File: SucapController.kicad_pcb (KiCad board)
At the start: 2 copper layers, 39.2 x 30.4 mm, 44 parts, among them J1 Conn_01x14, J2 Conn_01x04, J3 Conn_01x02, J4 Conn_02x03_Counter_Clockwise, J5 Conn_02x03_Counter_Clockwise, J6 Conn_02x03_Counter_Clockwise, J7 Screw_Terminal_01x01, Q1 SL2301, U1 HX9193, U2 HX9193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

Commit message: Do some change
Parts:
- removed Ce: 2.2u, Capacitor_SMD:C_0603_1608Metric
- removed D1: LED, LED_SMD:LED_0603_1608Metric
- removed J2: Conn_01x04, Connector_JST:JST_GH_SM04B-GHS-TB_1x04-1MP_P1.25mm_Horizontal
- added C19: 100n, GENERAL_RCL_SMD:C0603(1608M), F.Cu at (225.2, 97.7)
- C1, C11, C12, C13, C18, C2, C3, C4, C5, C6, C8, C9: footprint Capacitor_SMD:C_0603_1608Metric -> GENERAL_RCL_SMD:C0603(1608M)
- C17: value 100n -> 2.2u; footprint Capacitor_SMD:C_0603_1608Metric -> GENERAL_RCL_SMD:C0603(1608M)
- C7: footprint Capacitor_SMD:C_0603_1608Metric -> GENERAL_RCL_SMD:C0603(1608M); moved to F.Cu
- Q1: value SL2301 -> SI2301
- R1: value 10K -> 100n; footprint Resistor_SMD:R_0603_1608Metric -> GENERAL_RCL_SMD:R0603(1608M)
- R3: value 1K -> 1k; footprint Resistor_SMD:R_0603_1608Metric -> GENERAL_RCL_SMD:R0603(1608M)
- U1: value HX9193 -> HX9193-33GB; footprint Package_TO_SOT_SMD:SOT-23-5_HandSoldering -> GENERAL_SMALL-SEMI_SMD:SOT-23-5
- U4: value STM32H750VBTx -> STM32H750VBT6; footprint Package_QFP:LQFP-100_14x14mm_P0.5mm -> GENERAL_LARGE-SEMI_SMD:QFP-1414_100
- moved C13 59.8 mm to (249.0, 92.9), turned to 0 degrees
- moved C9 50.9 mm to (241.3, 95.4), turned to 0 degrees
- moved C11 46.5 mm to (237.8, 97.2), turned to 0 degrees
- moved C6 45.5 mm to (244.8, 98.0), turned to 0 degrees
- moved C3 45.3 mm to (241.3, 100.5), turned to 0 degrees
- moved C1 42.8 mm to (241.3, 98.0), turned to 0 degrees
- moved C2 41.7 mm to (229.8, 105.3)
- moved C18 38.7 mm to (244.8, 95.4), turned to 0 degrees
- moved C4 38.5 mm to (248.3, 95.4), turned to 0 degrees
- moved C5 24.7 mm to (237.8, 99.7), turned to 0 degrees
- moved C17 23.2 mm to (208.9, 110.3), turned to 180 degrees
- moved C7 20.7 mm to (214.2, 92.4), turned to 180 degrees
- moved C12 10.5 mm to (178.3, 107.4), turned to 0 degrees
- moved R1 6.88 mm to (198.7, 96.3), turned to 90 degrees
- moved U1 0.53 mm to (188.8, 108.8), turned to -90 degrees
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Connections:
- C17 pad 1: GND -> Net-(U4-Pad48)
- C17 pad 2: /RESET -> GND
- C18 pad 1: Net-(C18-Pad1) -> Net-(U4-Pad73)
- R1 pad 1: /RESET -> Net-(U4-Pad14)
- R3 pad 1: +3V3 -> Net-(D1-Pad2)
- R3 pad 2: Net-(D1-Pad2) -> +3V3
- U4 pad 14: /RESET -> Net-(U4-Pad14)
- U4 pad 48: Net-(C18-Pad1) -> Net-(U4-Pad48)
- U4 pad 73: Net-(C19-Pad1) -> Net-(U4-Pad73)
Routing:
- net Net-(U4-Pad48): track 0.00 -> 2.70 mm
- net Net-(C18-Pad1): track 2.70 -> 0.00 mm
- net Net-(U4-Pad73): track 0.00 -> 2.26 mm
- net Net-(C19-Pad1): track 2.26 -> 0.00 mm
- net +5V: track 63.8 -> 64.4 mm

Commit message: do some change
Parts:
- added D1: LED, GENERAL_2-PIN_PLASTIC_SMD:LED0603(1608M), F.Cu at (188.1, 98.2)
- C10, C14, C15, C16, C20, C21, C22: footprint Capacitor_SMD:C_0603_1608Metric -> GENERAL_RCL_SMD:C0603(1608M)
- C6: moved to B.Cu
- R2: footprint Resistor_SMD:R_0603_1608Metric -> GENERAL_RCL_SMD:R0603(1608M)
- U2: footprint Package_TO_SOT_SMD:SOT-23-5_HandSoldering -> GENERAL_SMALL-SEMI_SMD:SOT-23-5
- U3: footprint Package_SO:SOIC-8_5.23x5.23mm_P1.27mm -> GENERAL_MIDDLE-SEMI_SMD:SOIC-5252_8
- moved C13 61.6 mm to (188.5, 105.0), turned to -90 degrees
- moved C9 50.8 mm to (192.9, 110.8), turned to 180 degrees
- moved C4 48.5 mm to (200.1, 89.9), turned to 180 degrees
- moved C6 47.0 mm to (198.4, 105.8)
- moved C11 46.5 mm to (192.8, 109.2), turned to 180 degrees
- moved C1 45.9 mm to (196.5, 108.1), turned to 90 degrees
- moved C2 41.7 mm to (190.9, 90.6)
- moved C5 39.0 mm to (200.3, 110.4), turned to 180 degrees
- moved C3 30.1 mm to (212.4, 109.1), turned to 90 degrees
- moved C18 29.4 mm to (215.4, 94.4)
- moved C19 28.7 mm to (197.5, 90.2), turned to -90 degrees
- moved C12 12.2 mm to (190.3, 105.0), turned to -90 degrees
- moved R1 6.88 mm to (195.1, 90.4), turned to 180 degrees
- moved C20 1.68 mm to (201.2, 95.6), turned to 0 degrees
- turned U2 to -90 degrees
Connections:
- net Net-(U4-Pad14) renamed /RNSET
- C23 pad 1: GND -> /OSC32_IN
- C23 pad 2: /OSC32_IN -> GND
- C24 pad 1: GND -> /OSC32_OUT
- C24 pad 2: /OSC32_OUT -> GND
- U6 pad 4: /UART1_RX -> unconnected-(U6-Pad4)
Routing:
- net /RNSET: track 0.00 -> 24.4 mm
- net /RESET: track 24.4 -> 0.00 mm
- net GND: track 29.4 -> 17.6 mm, vias 32 -> 24
- net /OSC32_OUT: track 9.65 -> 21.4 mm, vias 0 -> 8

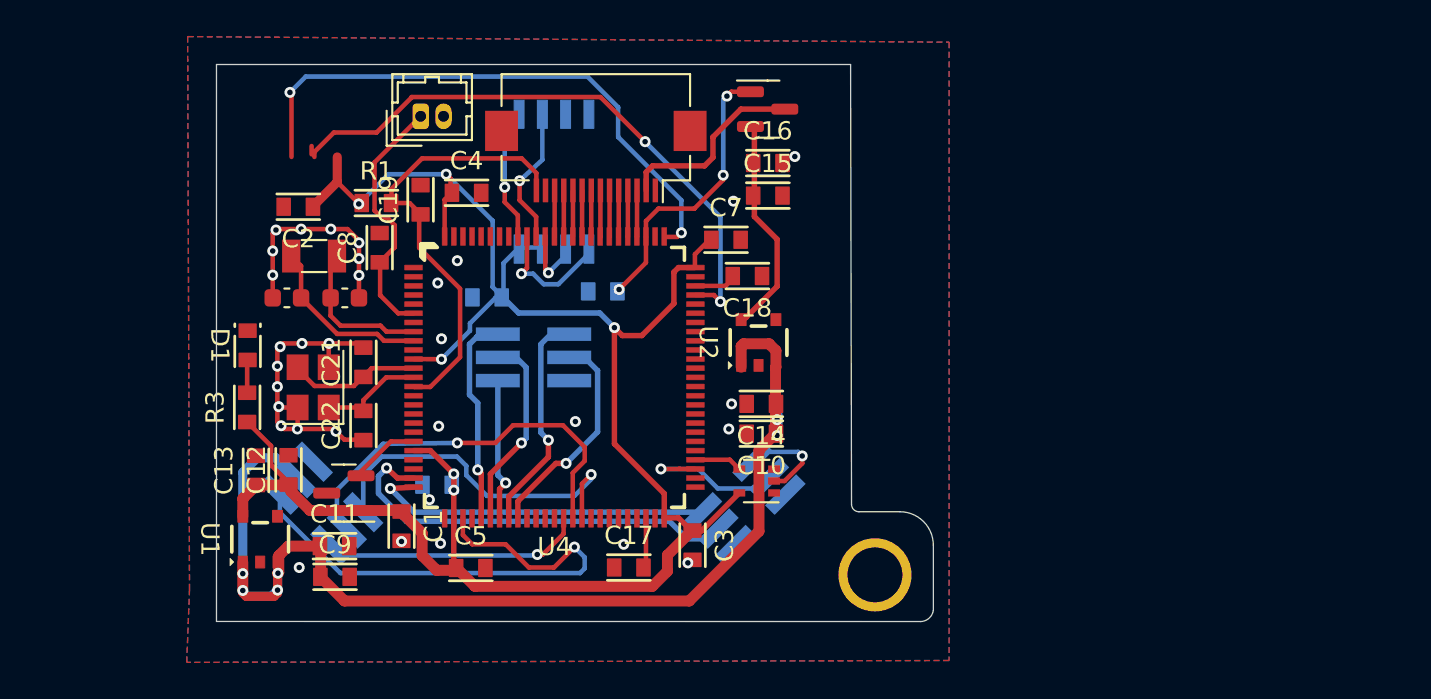
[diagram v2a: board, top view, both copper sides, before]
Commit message: Turn the footprints into ours
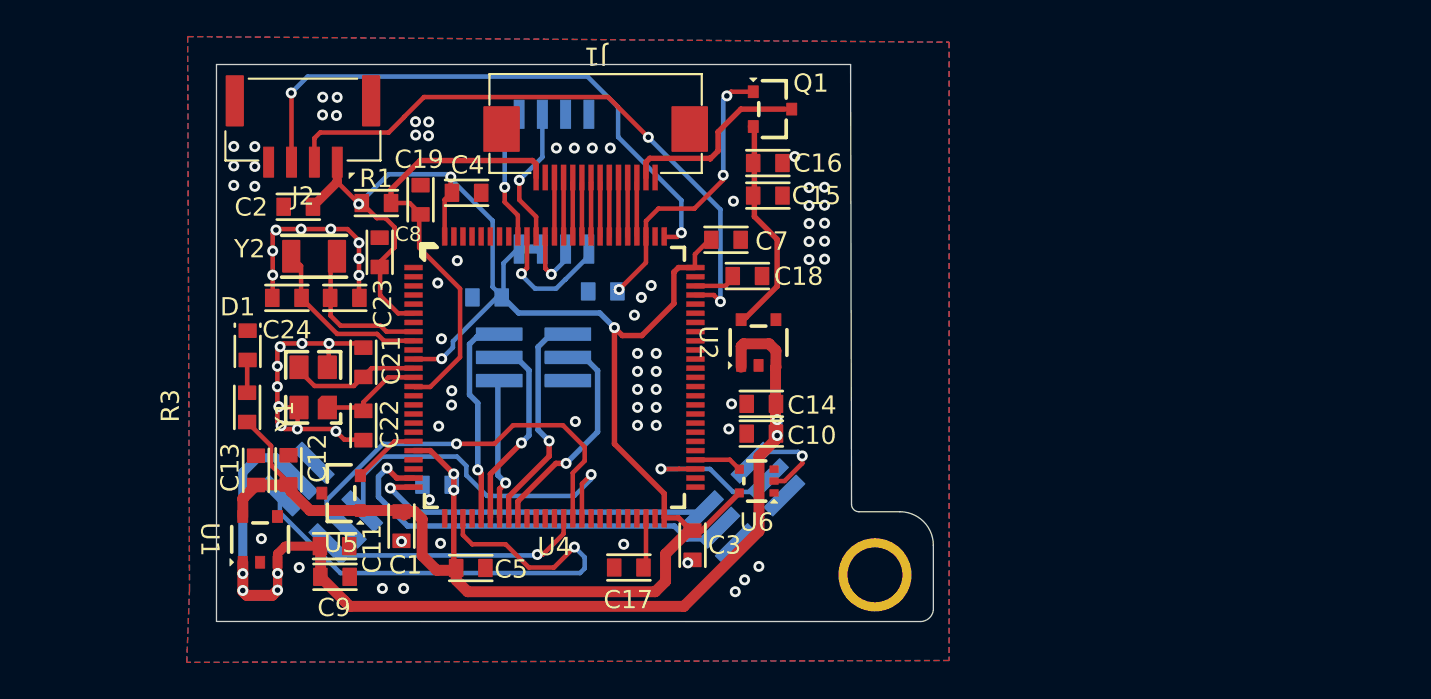
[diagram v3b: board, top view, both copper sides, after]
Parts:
- removed J3: Conn_01x02, Connector_Hirose:Hirose_DF13-02P-1.25DSA_1x02_P1.25mm_Vertical
- added J2: , CONNECTOR_GH_SMD:GH1.25_H_4, F.Cu at (191.1, 86.2)
- C23, C24: footprint Capacitor_SMD:C_0603_1608Metric -> GENERAL_RCL_SMD:C0603(1608M)
- J1: footprint Connector_FFC-FPC:Hirose_FH12-14S-0.5SH_1x14-1MP_P0.50mm_Horizontal -> MECHANICAL_EDGE-CONN:FFC_14
- J4, J5, J6: footprint Connector_PinHeader_1.27mm:PinHeader_2x03_P1.27mm_Vertical_SMD -> CONNECTOR_PINHEADER_SMD:PINHEADER_02x03_1.27mm
- Q1, U5: footprint Package_TO_SOT_SMD:SOT-23 -> GENERAL_SMALL-SEMI_SMD:SOT-23
- U6: footprint Package_TO_SOT_SMD:SOT-353_SC-70-5 -> GENERAL_SMALL-SEMI_SMD:SOT-353
- Y1: footprint Crystal:Crystal_SMD_3225-4Pin_3.2x2.5mm -> GENERAL_XTAL_OSC_SMD:SMD-3225_4
- Y2: footprint Crystal:Crystal_SMD_3215-2Pin_3.2x1.5mm -> GENERAL_XTAL_OSC_SMD:SMD-3215_2
- moved J1 1.80 mm to (207.1, 86.1)
- moved Q1 0.27 mm to (216.8, 85.3), turned to 180 degrees
- moved C8 0.25 mm to (195.3, 93.1)
- moved U5 0.15 mm to (193.2, 106.3), turned to 0 degrees
- turned U6 to 0 degrees
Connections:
- C19 pad 2: /RNSET -> /RESET
- C23 pad 1: /OSC32_IN -> GND
- C23 pad 2: GND -> /OSC32_IN
- C24 pad 1: /OSC32_OUT -> GND
- C24 pad 2: GND -> /OSC32_OUT
- C8 pad 2: +3V0 -> +3V3
- R1 pad 1: /RNSET -> /RESET
- U4 pad 14: /RNSET -> /RESET
- U4 pad 6: +3V0 -> +3V3
- U6 pad 1: (no net) -> unconnected-(U6-Pad1)
- U6 pad 4: unconnected-(U6-Pad4) -> /UART1_RX
- Y2 pad 1: /OSC32_IN -> /OSC32_OUT
- Y2 pad 2: /OSC32_OUT -> /OSC32_IN
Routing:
- net /RNSET: track 24.4 -> 0.00 mm
- net /RESET: track 0.00 -> 23.9 mm
- net +3V0: track 14.0 -> 0.00 mm
- net GND: track 17.6 -> 29.4 mm, vias 24 -> 81
- net /OSC32_OUT: track 21.4 -> 9.65 mm, vias 8 -> 0
- net +3V3: track 108.9 -> 118.9 mm
- net +5V: track 64.6 -> 63.9 mm
- net /SPI1_MOSI: track 7.08 -> 7.67 mm

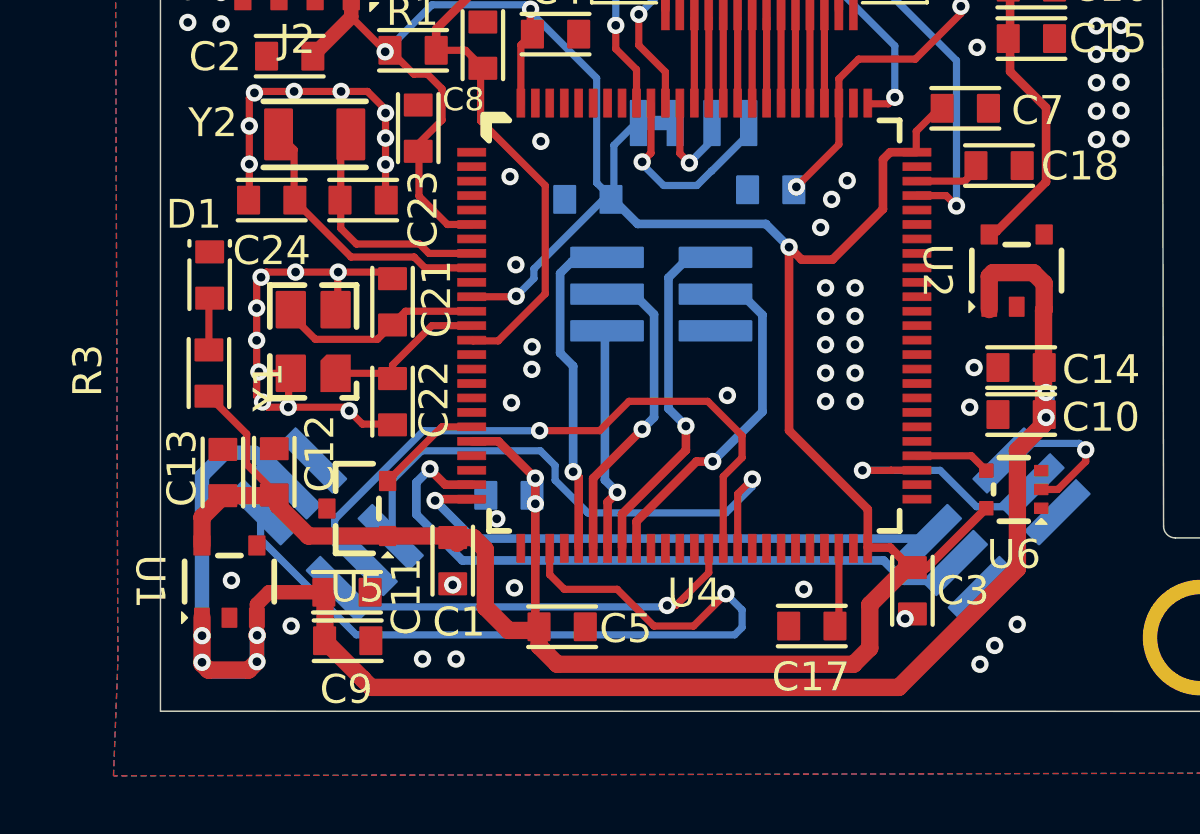
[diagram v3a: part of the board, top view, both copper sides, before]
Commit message: Turn REF3030 into TL431
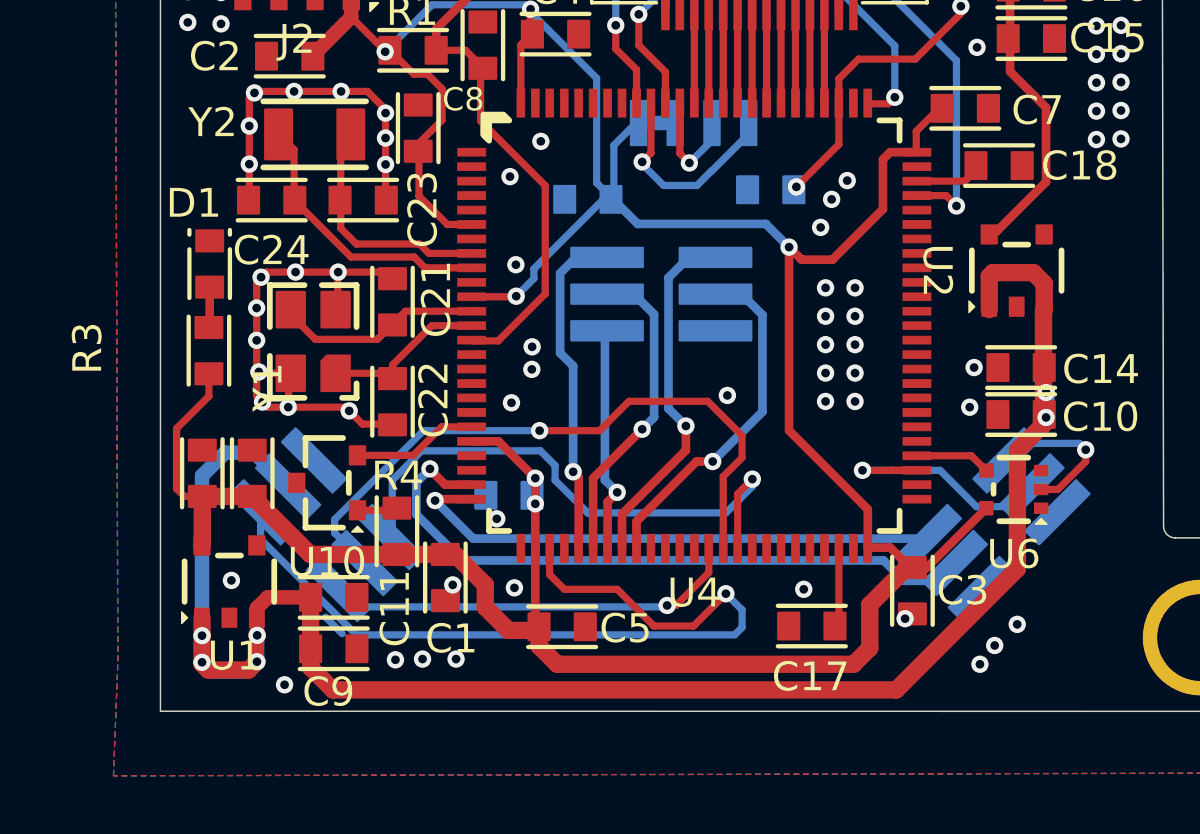
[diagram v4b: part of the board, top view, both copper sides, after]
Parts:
- removed U5: REF3030, GENERAL_SMALL-SEMI_SMD:SOT-23
- added R4: Resistor, GENERAL_RCL_SMD:R0603(1608M), F.Cu at (194.6, 107.1)
- added U10: TL431, GENERAL_SMALL-SEMI_SMD:SOT-23, F.Cu at (192.2, 105.4)
-  : renamed from C12
-  : renamed from C13
- moved R3 0.77 mm to (188.1, 100.8)
- moved   0.76 mm to (189.6, 105.1)
- moved   0.71 mm to (187.8, 105.1)
- moved C1 0.64 mm to (196.2, 108.7)
- moved C9 0.56 mm to (192.4, 111.1)
- moved C11 0.49 mm to (192.4, 109.3)
- moved D1 0.38 mm to (188.1, 97.8)
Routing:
- net Net-(U10-Pad1): track 0.00 -> 1.39 mm
- net GND: vias 81 -> 82

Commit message: fix some error
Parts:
-  : renamed from J1
-  : renamed from J7; footprint MyLib:TestPoint -> GENERAL_HOLE:HOLE-04-03_1
- C12, C13: renamed from  
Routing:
- net /EN_MOS: track 14.3 -> 13.5 mm
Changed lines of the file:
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@@
   (net 96 "Net-(J1-Pad2)")
   (net 97 "unconnected-(U6-Pad1)")
-  (net 98 "Net-(U10-Pad1)")
+  (net 98 "Net-(R4-Pad2)")
   (footprint "GENERAL_RCL_SMD:C0603(1608M)" (layer "F.Cu")
     (at 189.5602 105.0544 -90)
@@
     (property "Sheetname" "")
     (attr smd)
-    (fp_text reference " " (at -0.4318 -1.3462 90) (layer "F.SilkS")
+    (fp_text reference "C12" (at -0.4318 -1.3462 90) (layer "F.SilkS")
       (effects (font (size 1 1) (thickness 0.15)))
     )
@@
     (property "Sheetname" "")
     (attr smd)
-    (fp_text reference "J1" (at 0 3.683 180 unlocked) (layer "F.SilkS")
+    (fp_text reference " " (at 0 3.683 180 unlocked) (layer "F.SilkS")
       (effects (font (size 1 1) (thickness 0.15)))
     )
@@
     (fp_rect (start -0.65 -1.45) (end 0.65 1.45) (layer "F.Fab") (width 0.1) (fill none))
     (pad "1" smd roundrect (at 1.05 0.95 90) (size 0.7 0.6) (layers "F.Cu" "F.Paste" "F.Mask") (roundrect_rratio 0.05)
-      (net 98 "Net-(U10-Pad1)") (pinfunction "R") (pintype "power_in") (solder_mask_margin 0.05) (solder_paste_margin_ratio -0.075))
+      (net 98 "Net-(R4-Pad2)") (pinfunction "R") (pintype "power_in") (solder_mask_margin 0.05) (solder_paste_margin_ratio -0.075))
     (pad "2" smd roundrect (at 1.05 -0.95 90) (size 0.7 0.6) (layers "F.Cu" "F.Paste" "F.Mask") (roundrect_rratio 0.05)
       (net 53 "/VREF") (pinfunction "K") (pintype "power_out") (solder_mask_margin 0.05) (solder_paste_margin_ratio -0.075))
@@
     (property "Sheetname" "")
     (attr smd)
-    (fp_text reference "R3" (at -0.0872 4.1916 90) (layer "F.SilkS")
+    (fp_text reference "R3" (at 0.1016 1.3462 90) (layer "F.SilkS")
       (effects (font (size 1 1) (thickness 0.15)))
     )
@@
     (property "Sheetname" "")
     (attr smd)
-    (fp_text reference "Y1" (at -1.5746 -1.5584 90 unlocked) (layer "F.SilkS")
+    (fp_text reference "Y1" (at -2.2476 -2.667 90 unlocked) (layer "F.SilkS")
       (effects (font (size 1 1) (thickness 0.15)))
     )
@@
     )
   )
-  (footprint "MyLib:TestPoint" (layer "F.Cu")
+  (footprint "GENERAL_HOLE:HOLE-04-03_1" (layer "F.Cu")
     (at 222.3632 110.738)
     (property "Sheetfile" "SucapController.kicad_sch")
     (property "Sheetname" "")
-    (attr through_hole)
-    (fp_text reference "J7" (at 0.635 -1.905 unlocked) (layer "F.SilkS") hide
-      (effects (font (size 1 1) (thickness 0.15)))
-    )
-    (fp_text value "Screw_Terminal_01x01" (at 0 1 unlocked) (layer "F.Fab")
-      (effects (font (size 1 1) (thickness 0.15)))
-    )
-    (pad "1" thru_hole circle (at 0 0) (size 4 4) (drill 3) (layers *.Cu *.Mask)
+    (attr smd)
+    (fp_text reference " " (at 0 3.048 unlocked) (layer "F.SilkS")
+      (effects (font (size 1 1) (thickness 0.15)))
+    )
+    (fp_text value "Screw_Terminal_01x01" (at 0 -3.175 unlocked) (layer "F.Fab")
+      (effects (font (size 1 1) (thickness 0.15)))
+    )
+    (fp_text user "${REFERENCE}" (at 0 0 unlocked) (layer "F.Fab")
+      (effects (font (size 1 1) (thickness 0.15)))
+    )
+    (fp_line (start 0 -0.254) (end 0 0.254) (layer "F.Fab") (width 0.1))
+    (fp_line (start -0.254 0) (end 0.254 0) (layer "F.Fab") (width 0.1))
+    (pad "1" thru_hole circle (at -0.127 0) (size 4 4) (drill 3) (layers *.Cu *.Mask)
       (net 1 "GND") (pintype "passive"))
   )
@@
       (net 2 "+3V3") (pintype "passive") (solder_mask_margin 0.05) (solder_paste_margin_ratio -0.1))
     (pad "2" smd roundrect (at 0.8 0 180) (size 1 0.8) (layers "F.Cu" "F.Paste" "F.Mask") (roundrect_rratio 0.05)
-      (net 98 "Net-(U10-Pad1)") (pintype "passive") (solder_mask_margin 0.05) (solder_paste_margin_ratio -0.1))
+      (net 98 "Net-(R4-Pad2)") (pintype "passive") (solder_mask_margin 0.05) (solder_paste_margin_ratio -0.1))
     (model "${KICAD6_3RD_PARTY}/3dmodels/com_github_packagelan_packagelib/GENERAL_RCL_SMD.3dshapes/R_0603_1608Metric.wrl"
       (offset (xyz 0 0 0))
@@
     (property "Sheetname" "")
     (attr smd)
-    (fp_text reference "U2" (at 0 2.75 -90 unlocked) (layer "F.SilkS")
+    (fp_text reference "U2" (at 0.127 -2.6162 unlocked) (layer "F.SilkS")
       (effects (font (size 1 1) (thickness 0.15)))
     )
@@
     (property "Sheetname" "")
     (attr smd)
-    (fp_text reference " " (at -1.9558 -0.1778 180) (layer "F.SilkS")
+    (fp_text reference "C13" (at -1.9558 -0.1778 180) (layer "F.SilkS")
       (effects (font (size 1 1) (thickness 0.15)))
     )
@@
     (property "Sheetname" "")
     (attr smd)
-    (fp_text reference "J4" (at 0 -5.207 45 unlocked) (layer "B.SilkS")
+    (fp_text reference "J4" (at 0.035921 -3.232892 45 unlocked) (layer "B.SilkS")
       (effects (font (size 1 1) (thickness 0.15)) (justify mirror))
     )
@@
   (segment (start 202.184 109.0676) (end 203.454 110.3376) (width 0.25) (layer "F.Cu") (net 33))
   (via (at 205.9432 109.22) (size 0.6) (drill 0.3) (layers "F.Cu" "B.Cu") (net 33))
-  (segment (start 189.848716 106.351567) (end 189.848716 107.333767) (width 0.25) (layer "B.Cu") (net 33))
-  (segment (start 193.157349 110.6424) (end 206.248 110.6424) (width 0.25) (layer "B.Cu") (net 33))
+  (segment (start 206.502 109.7788) (end 205.9432 109.22) (width 0.25) (layer "B.Cu") (net 33))
+  (segment (start 192.4812 110.6424) (end 206.248 110.6424) (width 0.25) (layer "B.Cu") (net 33))
+  (segment (start 206.248 110.6424) (end 206.502 110.3884) (width 0.25) (layer "B.Cu") (net 33))
   (segment (start 206.502 110.3884) (end 206.502 109.7788) (width 0.25) (layer "B.Cu") (net 33))
-  (segment (start 206.248 110.6424) (end 206.502 110.3884) (width 0.25) (layer "B.Cu") (net 33))
-  (segment (start 189.848716 107.333767) (end 193.157349 110.6424) (width 0.25) (layer "B.Cu") (net 33))
-  (segment (start 206.502 109.7788) (end 205.9432 109.22) (width 0.25) (layer "B.Cu") (net 33))
+  (segment (start 190.9572 107.460051) (end 190.9572 109.1184) (width 0.25) (layer "B.Cu") (net 33))
+  (segment (start 189.848716 106.351567) (end 190.9572 107.460051) (width 0.25) (layer "B.Cu") (net 33))
+  (segment (start 190.9572 109.1184) (end 192.4812 110.6424) (width 0.25) (layer "B.Cu") (net 33))
   (segment (start 204.216 109.6264) (end 203.9112 109.6264) (width 0.25) (layer "F.Cu") (net 34))
   (segment (start 205.351 107.624) (end 205.351 108.4914) (width 0.25) (layer "F.Cu") (net 34))
   (segment (start 205.351 108.4914) (end 204.216 109.6264) (width 0.25) (layer "F.Cu") (net 34))
   (via (at 203.9112 109.6264) (size 0.6) (drill 0.3) (layers "F.Cu" "B.Cu") (net 34))
-  (segment (start 192.1002 110.0328) (end 192.668116 110.600716) (width 0.25) (layer "B.Cu") (net 34))
   (segment (start 193.174349 109.6772) (end 203.8604 109.6772) (width 0.25) (layer "B.Cu") (net 34))
   (segment (start 203.8604 109.6772) (end 203.9112 109.6264) (width 0.25) (layer "B.Cu") (net 34))
